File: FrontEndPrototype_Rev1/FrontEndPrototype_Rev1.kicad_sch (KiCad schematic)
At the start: 5 parts, among them J12 Conn_02x02_Odd_Even

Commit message: Checking if Branch Updates Work
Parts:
- renumbered Cb7 to Cb23, J12 to J15

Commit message: Small Updates
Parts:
- removed J15: Conn_02x02_Odd_Even, Connector_PinHeader_2.54mm:PinHeader_1x04_P2.54mm_Vertical_SMD_Pin1Right, symbol Connector_Generic:Conn_01x04
- removed TP1, TP2, TP3: TestPoint, TestPoint:TestPoint_Keystone_5015_Micro-Minature, symbol Connector:TestPoint
- added R10, R16, R17: 33, Resistor_SMD:R_0603_1608Metric_Pad0.98x0.95mm_HandSolder, symbol Device:R_Small_US
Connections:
- net DataOut1: now also R17.2
- net Dataout0: now also R16.1
- net V_SIG: now also R10.2
- new net MCU Connections/PA1: R10.1
- new net MCU Connections/PA6: R16.2
- new net MCU Connections/PA7: R17.1
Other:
- sheet MCU Connections ports: added PA3, PA4, PA5, PA6, PA7; removed PA15, QSPI_IO0, QSPI_IO1, QSPI_IO2, QSPI_IO3, QSPI_SCK, Tim2_PWM_2, Tim2_PWM_3
- note removed: "Test Points"

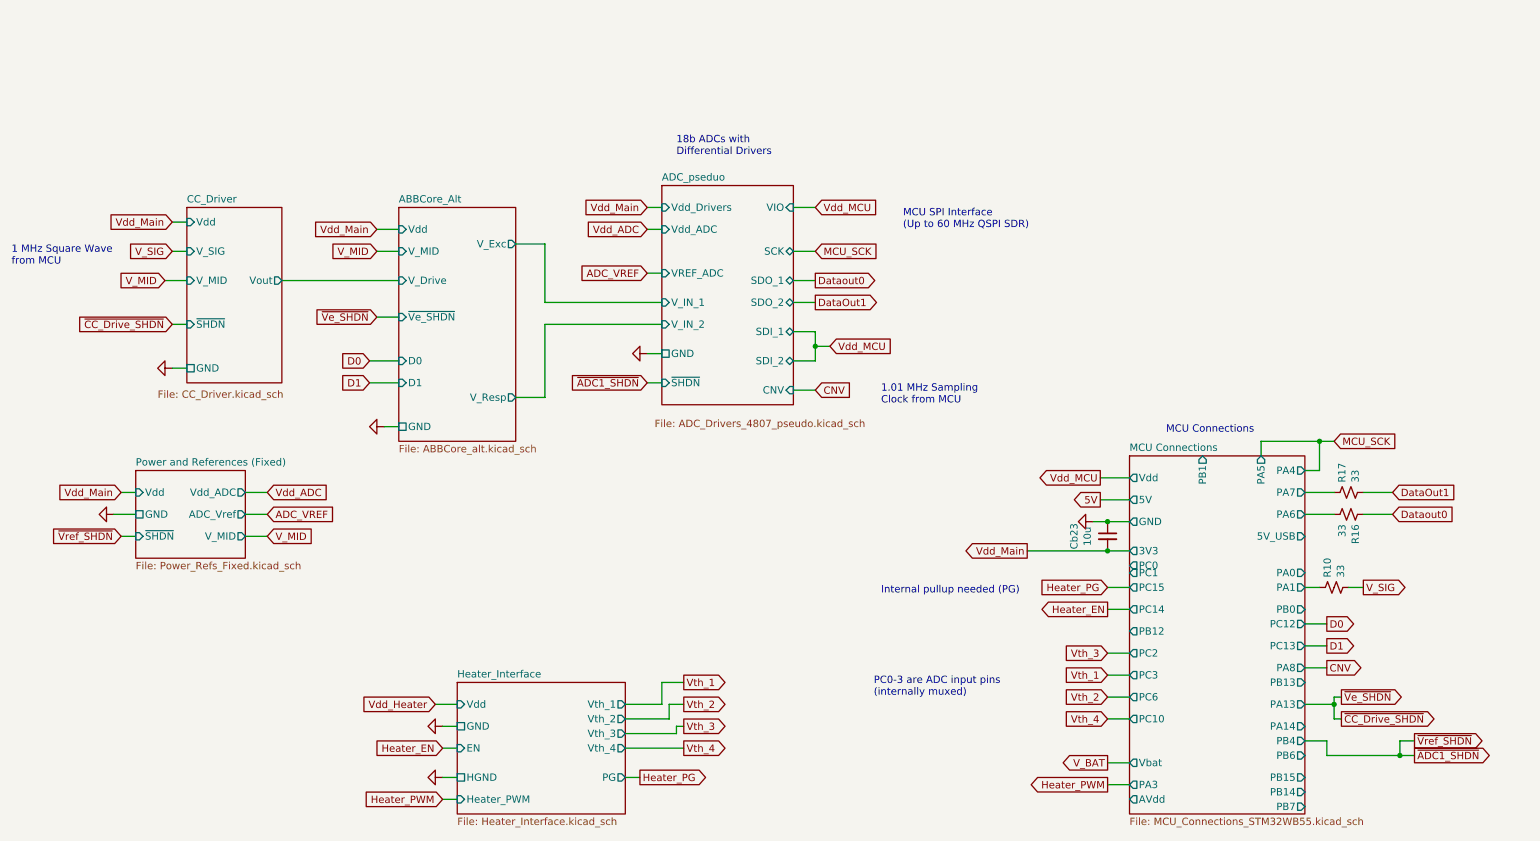
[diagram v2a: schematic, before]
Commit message: First Pass Schematic Fixes for Power Management Board
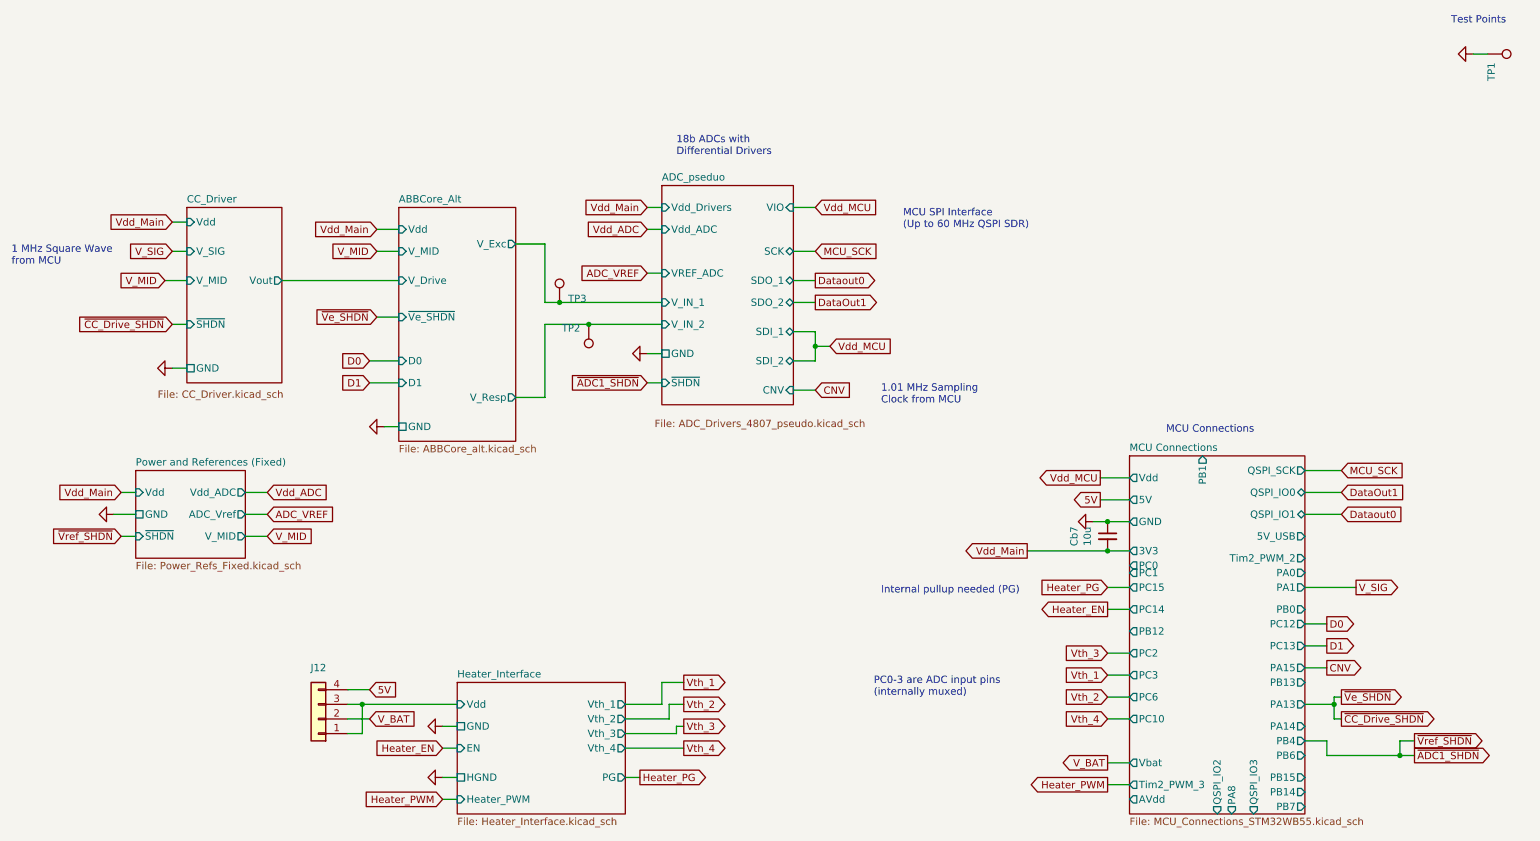
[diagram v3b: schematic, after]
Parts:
- removed R10, R16, R17: 33, Resistor_SMD:R_0603_1608Metric_Pad0.98x0.95mm_HandSolder, symbol Device:R_Small_US
- added J12: Conn_02x02_Odd_Even, Connector_PinHeader_2.54mm:PinHeader_1x04_P2.54mm_Vertical_SMD_Pin1Right, symbol Connector_Generic:Conn_01x04
- added TP1, TP2, TP3: TestPoint, TestPoint:TestPoint_Keystone_5015_Micro-Minature, symbol Connector:TestPoint
- renumbered Cb23 to Cb7
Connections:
- net 5V: now also J12.4 (Pin_4)
- net ABBCore_Alt/V_Exc: now also TP3.1
- net ABBCore_Alt/V_Resp: now also TP2.1
- net GND: now also TP1.1
- net V_BAT: now also J12.2 (Pin_2)
- new net Heater_Interface/Vdd: J12.1 (Pin_1), J12.3 (Pin_3)
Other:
- sheet MCU Connections ports: added PA15, QSPI_IO0, QSPI_IO1, QSPI_IO2, QSPI_IO3, QSPI_SCK, Tim2_PWM_2, Tim2_PWM_3; removed PA3, PA4, PA5, PA6, PA7
- note added: "Test Points"

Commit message: Updated Measurement Board with new 3V Reference
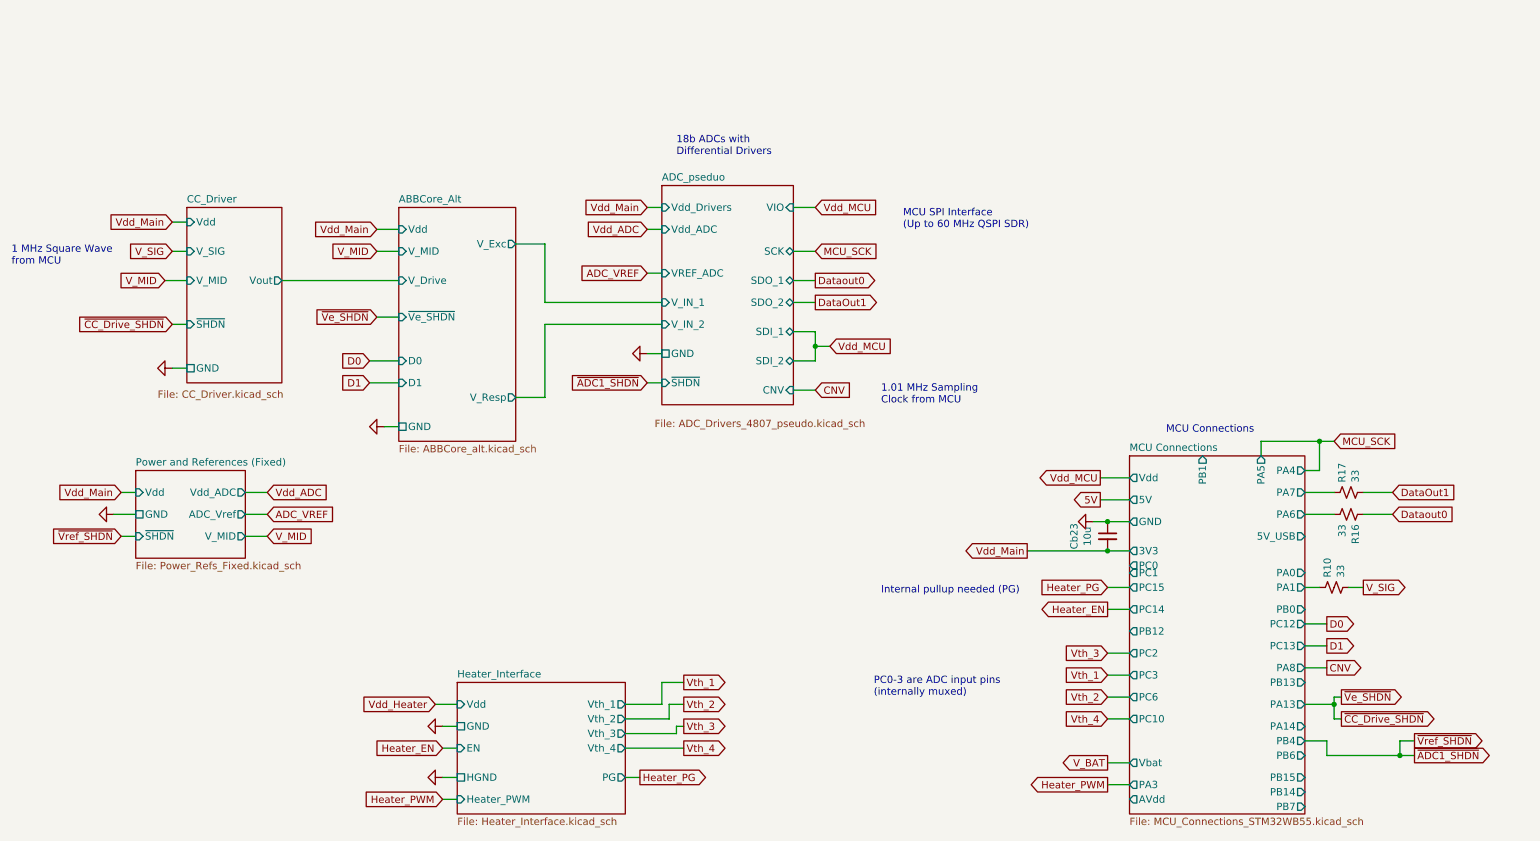
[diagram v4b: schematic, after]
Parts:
- removed J12: Conn_02x02_Odd_Even, Connector_PinHeader_2.54mm:PinHeader_1x04_P2.54mm_Vertical_SMD_Pin1Right, symbol Connector_Generic:Conn_01x04
- removed TP1, TP2, TP3: TestPoint, TestPoint:TestPoint_Keystone_5015_Micro-Minature, symbol Connector:TestPoint
- added R10, R16, R17: 33, Resistor_SMD:R_0603_1608Metric_Pad0.98x0.95mm_HandSolder, symbol Device:R_Small_US
- renumbered Cb7 to Cb23
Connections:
- net DataOut1: now also R17.2
- net Dataout0: now also R16.1
- net V_SIG: now also R10.2
- new net MCU Connections/PA1: R10.1
- new net MCU Connections/PA6: R16.2
- new net MCU Connections/PA7: R17.1
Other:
- sheet MCU Connections ports: added PA3, PA4, PA5, PA6, PA7; removed PA15, QSPI_IO0, QSPI_IO1, QSPI_IO2, QSPI_IO3, QSPI_SCK, Tim2_PWM_2, Tim2_PWM_3
- note removed: "Test Points"
